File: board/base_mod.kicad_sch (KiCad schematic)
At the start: 33 parts, among them J3 RS-232, J4 LCD, Q5 BC548, Q6 BC548, SW10 MENU, SW3 RI, SW4 UP, SW5 LE, SW6 OK, SW7 DN, SW8 CANCEL, SW9 BACK, U4 AT24C1024B, U5 MAX3232, U6 24LCxxx, U7 MCP23008-xP, U8 BOB-12009

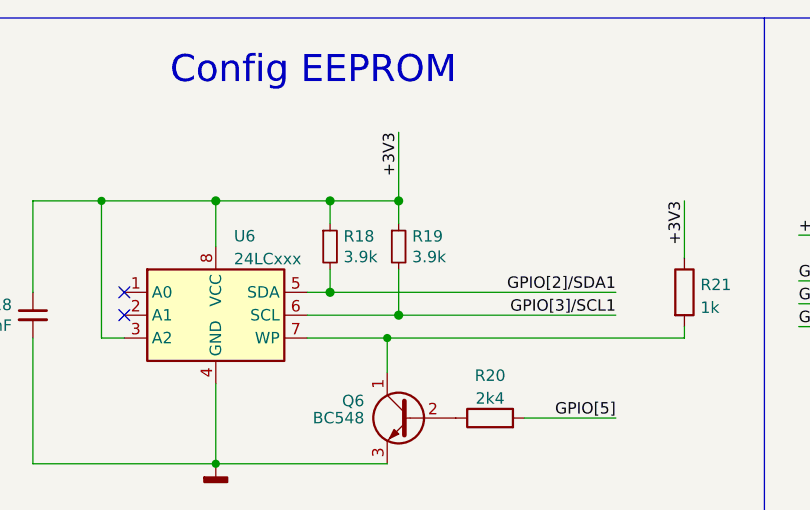
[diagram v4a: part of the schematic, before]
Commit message: Re-structure schematics and improve safety.
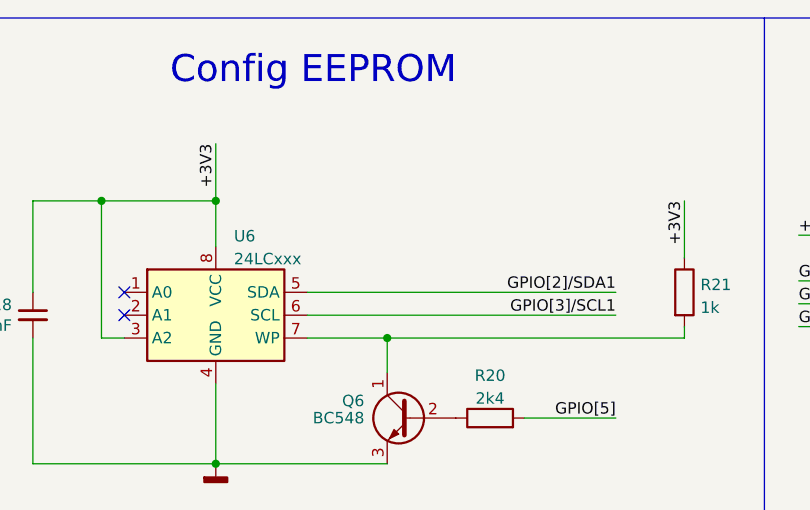
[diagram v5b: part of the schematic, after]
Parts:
- removed R18, R19: 3.9k, symbol Device:R_Small
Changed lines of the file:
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@@
   (junction (at 38.1 33.02) (diameter 0) (color 0 0 0 0)
   )
-  (junction (at 140.97 33.02) (diameter 1.016) (color 0 0 0 0)
-  )
-  (junction (at 133.35 33.02) (diameter 1.016) (color 0 0 0 0)
-  )
-  (junction (at 120.65 33.02) (diameter 1.016) (color 0 0 0 0)
-  )
   (junction (at 261.62 139.7) (diameter 0) (color 0 0 0 0)
   )
@@
   (junction (at 191.77 139.7) (diameter 0) (color 0 0 0 0)
   )
-  (junction (at 140.97 45.72) (diameter 1.016) (color 0 0 0 0)
-  )
   (junction (at 107.95 33.02) (diameter 0) (color 0 0 0 0)
   )
   (junction (at 247.65 139.7) (diameter 0) (color 0 0 0 0)
   )
+  (junction (at 120.65 33.02) (diameter 0) (color 0 0 0 0)
+  )
   (junction (at 139.7 48.26) (diameter 0) (color 0 0 0 0)
   )
@@
   )
   (junction (at 157.48 127) (diameter 0) (color 0 0 0 0)
-  )
-  (junction (at 133.35 43.18) (diameter 1.016) (color 0 0 0 0)
   )
   (junction (at 270.51 109.22) (diameter 0) (color 0 0 0 0)
@@
     (stroke (width 0) (type default) (color 0 0 0 0))
   )
+  (wire (pts (xy 120.65 26.67) (xy 120.65 33.02))
+    (stroke (width 0) (type default) (color 0 0 0 0))
+  )
   (wire (pts (xy 162.56 124.46) (xy 157.48 124.46))
     (stroke (width 0) (type default) (color 0 0 0 0))
@@
     (stroke (width 0) (type default) (color 0 0 0 0))
   )
-  (wire (pts (xy 130.81 43.18) (xy 133.35 43.18))
+  (wire (pts (xy 130.81 43.18) (xy 165.1 43.18))
     (stroke (width 0) (type solid) (color 0 0 0 0))
   )
@@
     (stroke (width 0) (type default) (color 0 0 0 0))
   )
-  (wire (pts (xy 133.35 43.18) (xy 165.1 43.18))
-    (stroke (width 0) (type default) (color 0 0 0 0))
-  )
   (wire (pts (xy 157.48 106.68) (xy 162.56 106.68))
     (stroke (width 0) (type default) (color 0 0 0 0))
@@
     (stroke (width 0) (type solid) (color 0 0 0 0))
   )
-  (wire (pts (xy 130.81 45.72) (xy 140.97 45.72))
-    (stroke (width 0) (type solid) (color 0 0 0 0))
-  )
   (wire (pts (xy 69.85 92.71) (xy 69.85 88.9))
     (stroke (width 0) (type default) (color 0 0 0 0))
@@
     (stroke (width 0) (type default) (color 0 0 0 0))
   )
-  (wire (pts (xy 133.35 33.02) (xy 133.35 35.56))
-    (stroke (width 0) (type solid) (color 0 0 0 0))
-  )
   (wire (pts (xy 199.39 93.98) (xy 270.51 93.98))
     (stroke (width 0) (type default) (color 0 0 0 0))
@@
     (stroke (width 0) (type default) (color 0 0 0 0))
   )
-  (wire (pts (xy 140.97 40.64) (xy 140.97 45.72))
-    (stroke (width 0) (type solid) (color 0 0 0 0))
-  )
   (wire (pts (xy 261.62 128.27) (xy 261.62 111.76))
     (stroke (width 0) (type default) (color 0 0 0 0))
@@
     (stroke (width 0) (type default) (color 0 0 0 0))
   )
-  (wire (pts (xy 140.97 45.72) (xy 165.1 45.72))
+  (wire (pts (xy 130.81 45.72) (xy 165.1 45.72))
     (stroke (width 0) (type default) (color 0 0 0 0))
   )
@@
     (stroke (width 0) (type solid) (color 0 0 0 0))
   )
-  (wire (pts (xy 133.35 40.64) (xy 133.35 43.18))
-    (stroke (width 0) (type solid) (color 0 0 0 0))
-  )
   (wire (pts (xy 261.62 139.7) (xy 261.62 138.43))
     (stroke (width 0) (type default) (color 0 0 0 0))
@@
     (stroke (width 0) (type solid) (color 0 0 0 0))
   )
-  (wire (pts (xy 140.97 33.02) (xy 133.35 33.02))
-    (stroke (width 0) (type solid) (color 0 0 0 0))
-  )
   (wire (pts (xy 205.74 121.92) (xy 205.74 128.27))
     (stroke (width 0) (type default) (color 0 0 0 0))
@@
     (stroke (width 0) (type default) (color 0 0 0 0))
   )
-  (wire (pts (xy 120.65 33.02) (xy 133.35 33.02))
-    (stroke (width 0) (type solid) (color 0 0 0 0))
-  )
   (wire (pts (xy 107.95 33.02) (xy 107.95 48.26))
     (stroke (width 0) (type default) (color 0 0 0 0))
   )
-  (wire (pts (xy 140.97 35.56) (xy 140.97 33.02))
-    (stroke (width 0) (type solid) (color 0 0 0 0))
-  )
   (wire (pts (xy 199.39 106.68) (xy 199.39 105.41))
     (stroke (width 0) (type default) (color 0 0 0 0))
@@
   (wire (pts (xy 187.96 116.84) (xy 233.68 116.84))
     (stroke (width 0) (type default) (color 0 0 0 0))
-  )
-  (wire (pts (xy 140.97 25.4) (xy 140.97 33.02))
-    (stroke (width 0) (type solid) (color 0 0 0 0))
   )
   (wire (pts (xy 71.12 57.15) (xy 86.36 57.15))
@@
     (effects (font (size 1.27 1.27)) (justify left bottom))
   )
-  (label "+3V3" (at 140.97 25.4 270)
+  (label "+3V3" (at 120.65 26.67 270)
     (effects (font (size 1.27 1.27)) (justify right bottom))
   )
@@
     (pin "9")
   )
-  (symbol (lib_id "Device:R_Small") (at 133.35 38.1 0) (unit 1)
-    (in_bom yes) (on_board yes)
-    (property "Reference" "R18" (id 0) (at 134.8486 36.957 0)
-      (effects (font (size 1.27 1.27)) (justify left))
-    )
-    (property "Value" "3.9k" (id 1) (at 134.8487 39.2493 0)
-      (effects (font (size 1.27 1.27)) (justify left))
-    )
-    (property "Footprint" "" (id 2) (at 133.35 38.1 0)
-      (effects (font (size 1.27 1.27)) hide)
-    )
-    (property "Datasheet" "~" (id 3) (at 133.35 38.1 0)
-      (effects (font (size 1.27 1.27)) hide)
-    )
-    (pin "1")
-    (pin "2")
-  )
   (symbol (lib_id "Device:C_Polarized") (at 95.25 104.14 0) (unit 1)
     (in_bom yes) (on_board yes) (fields_autoplaced)
@@
     (pin "8")
   )
-  (symbol (lib_id "Device:R_Small") (at 140.97 38.1 0) (unit 1)
-    (in_bom yes) (on_board yes)
-    (property "Reference" "R19" (id 0) (at 142.4686 36.957 0)
-      (effects (font (size 1.27 1.27)) (justify left))
-    )
-    (property "Value" "3.9k" (id 1) (at 142.4687 39.2493 0)
-      (effects (font (size 1.27 1.27)) (justify left))
-    )
-    (property "Footprint" "" (id 2) (at 140.97 38.1 0)
-      (effects (font (size 1.27 1.27)) hide)
-    )
-    (property "Datasheet" "~" (id 3) (at 140.97 38.1 0)
-      (effects (font (size 1.27 1.27)) hide)
-    )
-    (pin "1")
-    (pin "2")
-  )
   (symbol (lib_id "Device:R") (at 151.13 57.15 90) (unit 1)

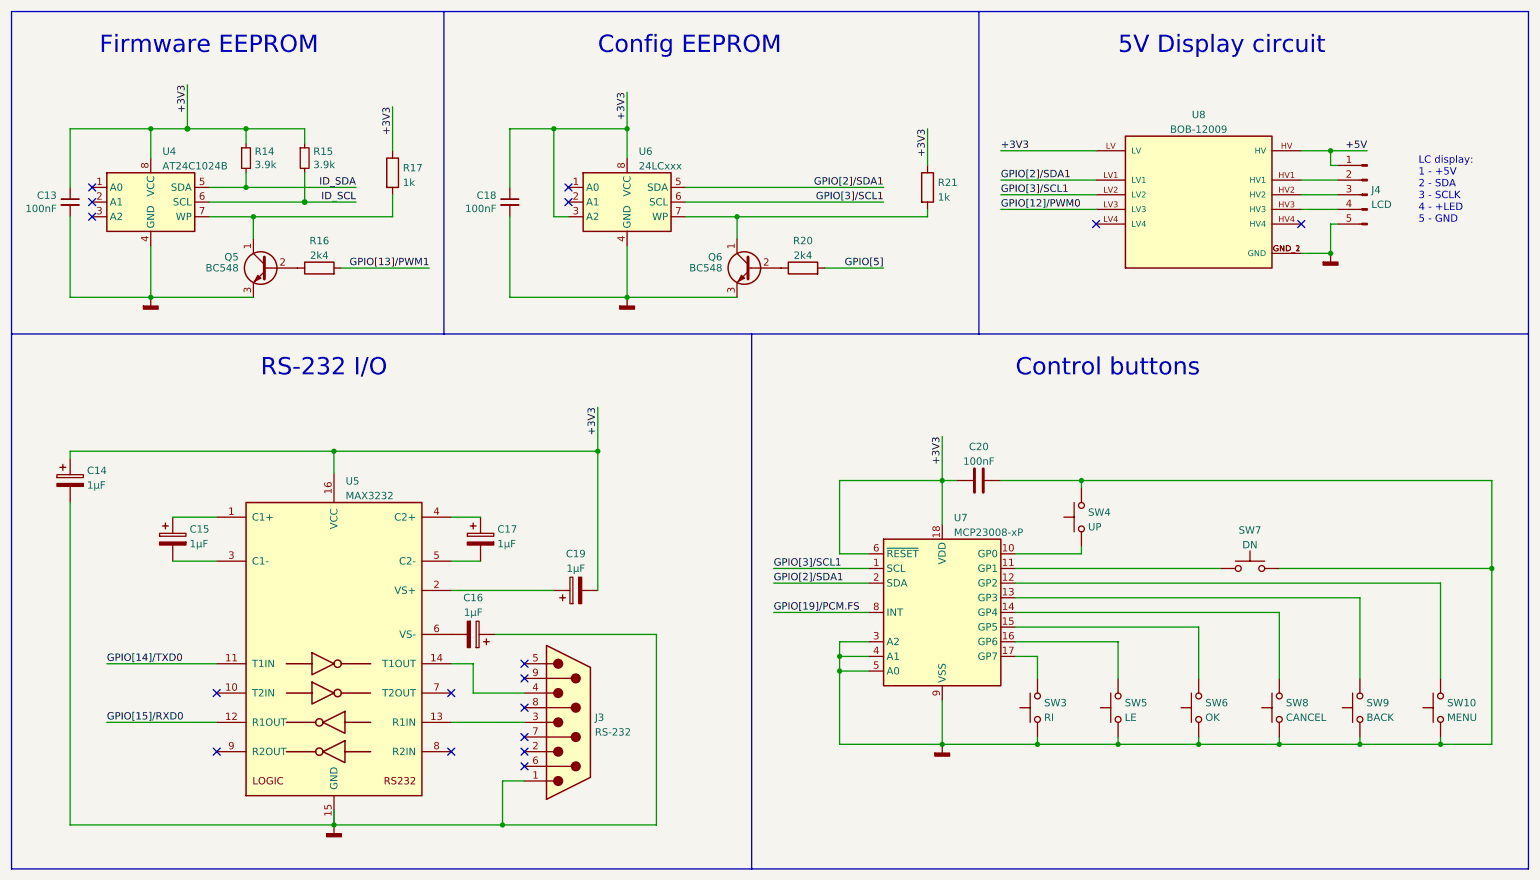
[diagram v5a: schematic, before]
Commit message: Add missing footprints.
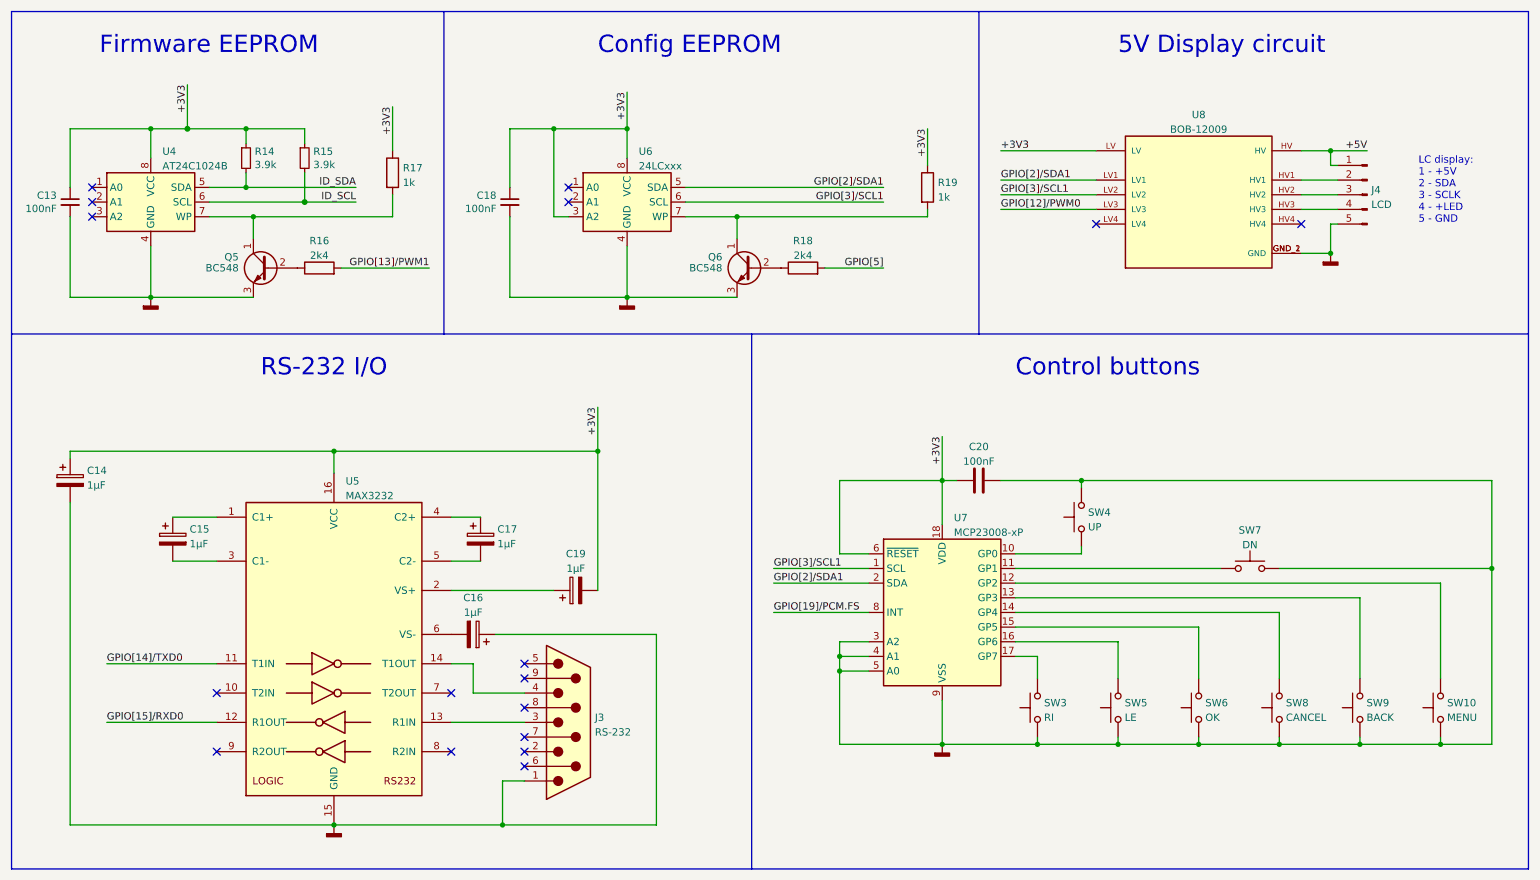
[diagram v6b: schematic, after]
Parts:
- C13, C14, C15, C16, C17, C19: footprint (none) -> Capacitor_THT:C_Radial_D6.3mm_H5.0mm_P2.50mm
- C18, C20: footprint (none) -> Capacitor_THT:C_Disc_D5.0mm_W2.5mm_P5.00mm
- R14, R15, R16, R17: footprint (none) -> Resistor_THT:R_Axial_DIN0516_L15.5mm_D5.0mm_P7.62mm_Vertical
- R18: renamed from R20; footprint (none) -> Resistor_THT:R_Axial_DIN0516_L15.5mm_D5.0mm_P7.62mm_Vertical
- R19: renamed from R21; footprint (none) -> Resistor_THT:R_Axial_DIN0516_L15.5mm_D5.0mm_P7.62mm_Vertical
- SW10, SW3, SW5, SW6, SW8, SW9: footprint Button_Switch_SMD:SW_MEC_5GSH9 -> Button_Switch_THT:SW_PUSH_6mm
- SW4, SW7: footprint (none) -> Button_Switch_THT:SW_PUSH_6mm
- U5: footprint (none) -> Package_DIP:DIP-16_W7.62mm_Socket_LongPads
- U6: footprint (none) -> Package_DIP:DIP-8_W7.62mm_Socket_LongPads

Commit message: Change net descriptors.
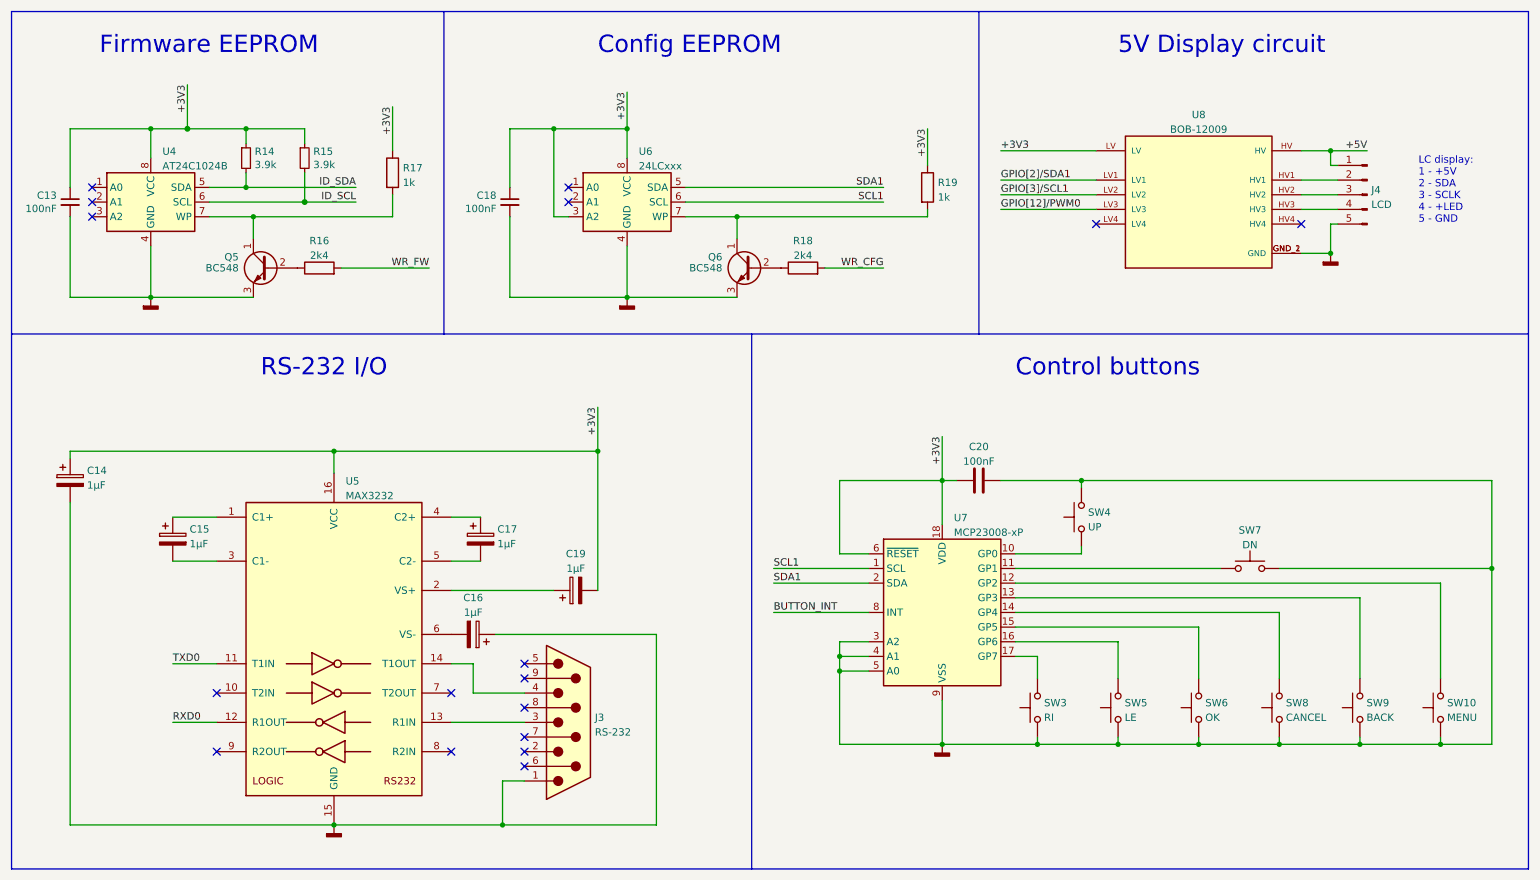
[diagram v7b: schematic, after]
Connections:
- net GPIO[2]/SDA1: no longer U6.5 (SDA), U7.2 (SDA)
- net GPIO[3]/SCL1: no longer U6.6 (SCL), U7.1 (SCL)
- net GPIO[13]/PWM1 renamed WR_FW
- net GPIO[14]/TXD0 renamed TXD0
- net GPIO[15]/RXD0 renamed RXD0
- net GPIO[19]/PCM.FS renamed BUTTON_INT
- net GPIO[5] renamed WR_CFG
- new net SCL1: U6.6 (SCL), U7.1 (SCL)
- new net SDA1: U6.5 (SDA), U7.2 (SDA)
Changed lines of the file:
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@@
   (no_connect (at 49.53 140.97))
   (no_connect (at 110.49 43.18))
-  (wire (pts (xy 30.48 135.89) (xy 49.53 135.89))
+  (wire (pts (xy 41.91 135.89) (xy 49.53 135.89))
     (stroke (width 0) (type default) (color 0 0 0 0))
   )
@@
     (stroke (width 0) (type default) (color 0 0 0 0))
   )
-  (wire (pts (xy 30.48 125.73) (xy 49.53 125.73))
+  (wire (pts (xy 41.91 125.73) (xy 49.53 125.73))
     (stroke (width 0) (type default) (color 0 0 0 0))
   )
@@
     (effects (font (size 3 3)) (justify left bottom))
   )
-  (label "GPIO[13]{slash}PWM1" (at 86.36 57.15 180)
+  (label "WR_FW" (at 86.36 57.15 180)
+    (effects (font (size 1.27 1.27)) (justify right bottom))
+  )
+  (label "SDA1" (at 165.1 43.18 180)
     (effects (font (size 1.27 1.27)) (justify right bottom))
   )
@@
     (effects (font (size 1.27 1.27)) (justify left bottom))
   )
-  (label "GPIO[3]{slash}SCL1" (at 165.1 45.72 180)
-    (effects (font (size 1.27 1.27)) (justify right bottom))
-  )
-  (label "GPIO[5]" (at 165.1 57.15 180)
-    (effects (font (size 1.27 1.27)) (justify right bottom))
-  )
-  (label "GPIO[3]{slash}SCL1" (at 146.05 109.22 0)
-    (effects (font (size 1.27 1.27)) (justify left bottom))
+  (label "TXD0" (at 41.91 125.73 0)
+    (effects (font (size 1.27 1.27)) (justify left bottom))
+  )
+  (label "WR_CFG" (at 165.1 57.15 180)
+    (effects (font (size 1.27 1.27)) (justify right bottom))
   )
   (label "+3V3" (at 115.57 81.28 270)
@@
     (effects (font (size 1.27 1.27)) (justify right bottom))
   )
-  (label "GPIO[14]{slash}TXD0" (at 30.48 125.73 0)
-    (effects (font (size 1.27 1.27)) (justify left bottom))
-  )
   (label "+3V3" (at 175.26 86.36 270)
     (effects (font (size 1.27 1.27)) (justify right bottom))
@@
     (effects (font (size 1.27 1.27)) (justify right bottom))
   )
-  (label "GPIO[19]{slash}PCM.FS" (at 146.05 116.84 0)
-    (effects (font (size 1.27 1.27)) (justify left bottom))
-  )
-  (label "GPIO[15]{slash}RXD0" (at 30.48 135.89 0)
-    (effects (font (size 1.27 1.27)) (justify left bottom))
-  )
-  (label "GPIO[2]{slash}SDA1" (at 146.05 111.76 0)
+  (label "SCL1" (at 165.1 45.72 180)
+    (effects (font (size 1.27 1.27)) (justify right bottom))
+  )
+  (label "BUTTON_INT" (at 146.05 116.84 0)
+    (effects (font (size 1.27 1.27)) (justify left bottom))
+  )
+  (label "SDA1" (at 146.05 111.76 0)
+    (effects (font (size 1.27 1.27)) (justify left bottom))
+  )
+  (label "SCL1" (at 146.05 109.22 0)
     (effects (font (size 1.27 1.27)) (justify left bottom))
   )
@@
     (effects (font (size 1.27 1.27)) (justify left bottom))
   )
-  (label "GPIO[2]{slash}SDA1" (at 165.1 43.18 180)
-    (effects (font (size 1.27 1.27)) (justify right bottom))
+  (label "RXD0" (at 41.91 135.89 0)
+    (effects (font (size 1.27 1.27)) (justify left bottom))
   )
   (label "ID_SDA" (at 73.66 43.18 180)
